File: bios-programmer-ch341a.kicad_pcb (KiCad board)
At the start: 2 copper layers, 50 x 56 mm, 28 parts, among them J1 USB_B_Micro, J4 +Banana+, J5 -Banana-, J6 ZIF16, J7 Conn_02x04_Counter_Clockwise, J8 Conn_02x04_Counter_Clockwise, SW1 RESET, U1 CH341A, U2 ISO6741, U3 ADuM1252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

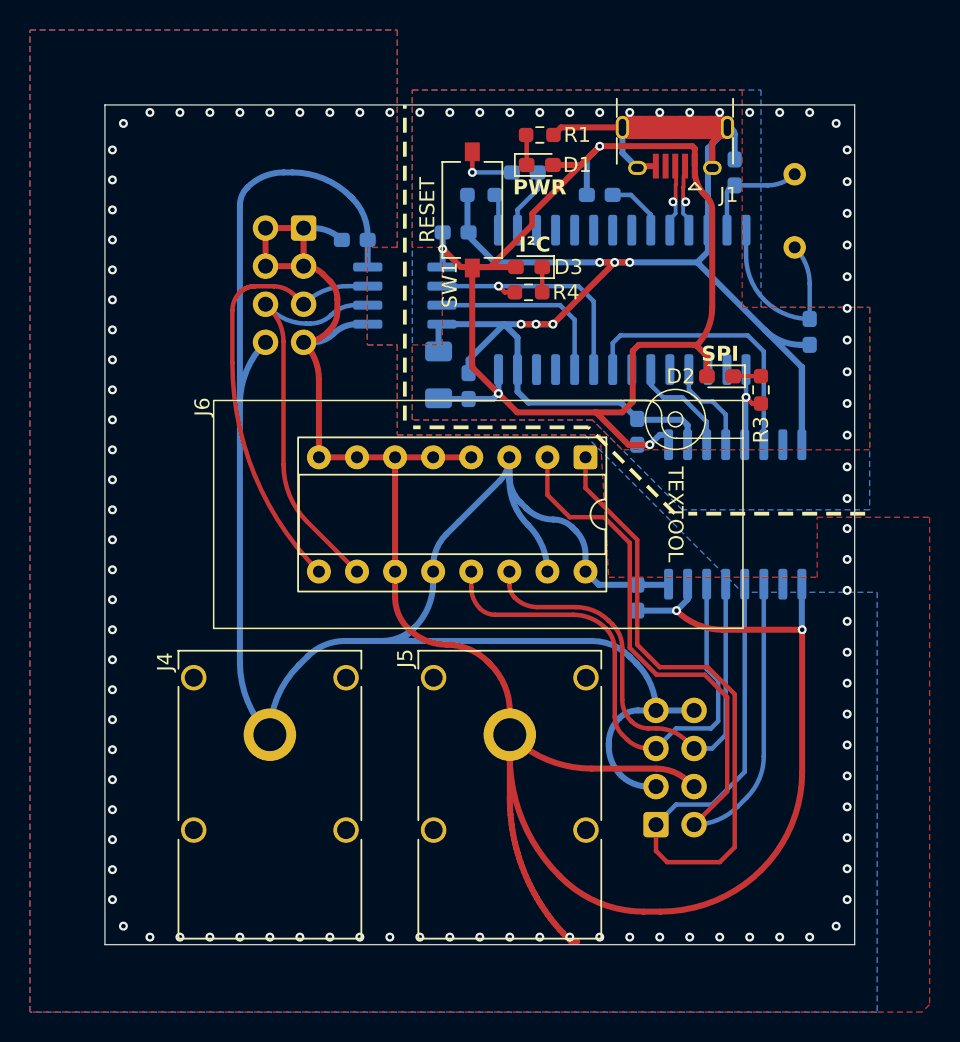
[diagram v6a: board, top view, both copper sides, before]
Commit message: PCB: added silkscreens for pin layout and found BIG ISSUE
These silkscreens are quite important simply to understand what the device does
and prevent mistakes. They need to be correct and placed in a way they can be
read easily without mistakes.

As I expected I seem to have made a mistake on at least the pinouts of the IDC
connectors. That's too bad since I'l have to reroute them after correcting this.
First things first however, I'm going to verify the pinout of both the IDC con-
nectors and the ZIF socket with every reference I have.

The worst thing that could happen - as it's hard to fix with an extra compoent
or a hookup wire - is a mistake in the pinouts. All of the PCBs that I order
will be a waste of both money and resources.
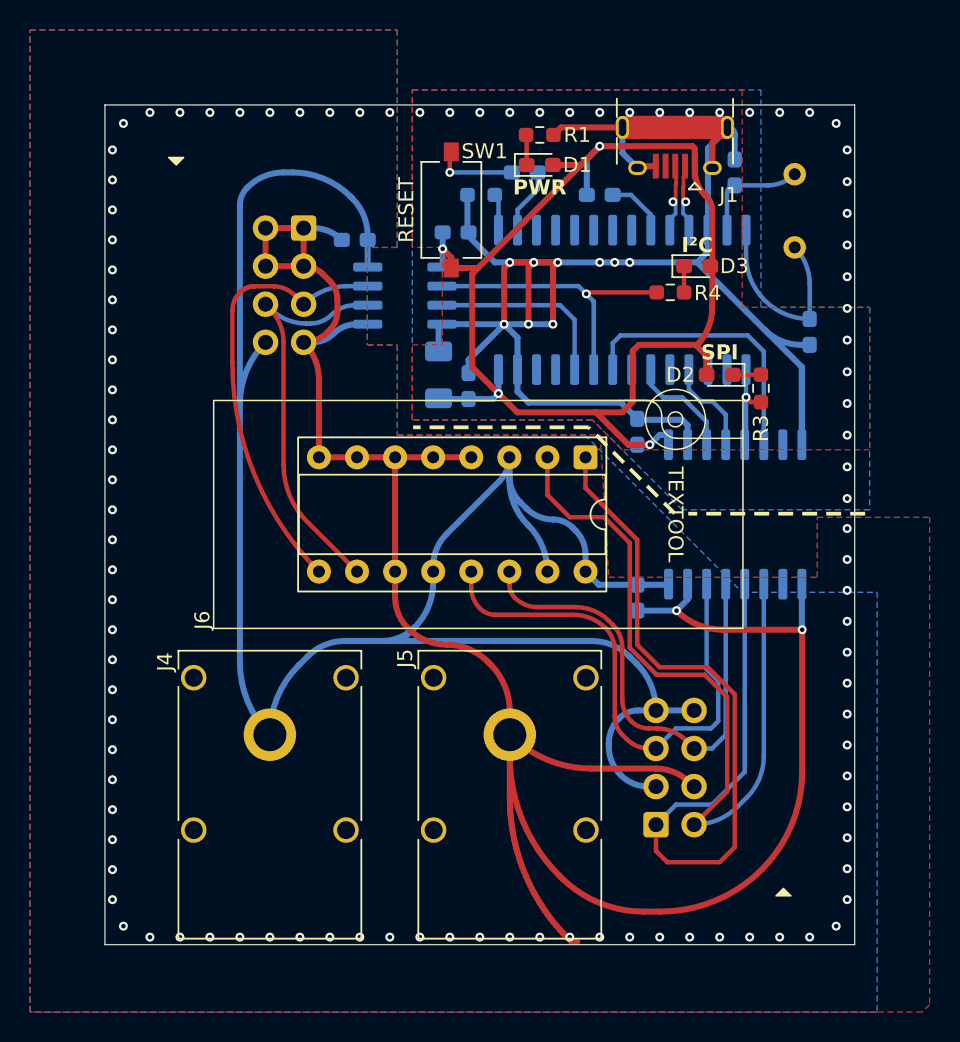
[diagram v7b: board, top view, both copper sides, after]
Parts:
- moved D3 11.2 mm to (79.5, 40.8), turned to 0 degrees
- moved R4 9.46 mm to (77.7, 42.5)
- moved SW1 1.40 mm to (63.1, 37.0)
- moved D2 0.10 mm to (81.0, 48.0)
- moved R3 0.10 mm to (83.8, 48.9)
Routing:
- net GND: track 222.2 -> 228.2 mm, vias 33 -> 36
- net /SDA: track 16.4 -> 19.8 mm
- net VBUS: track 88.6 -> 85.8 mm
- net /RST: track 4.01 -> 5.51 mm
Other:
- board text removed: "reset switch kleiner ring rondom rond, niet connected? of toch GND? maar welke? 2 halve ringen? misschien beter 2 zones, tot bijna tegen elkaar?"

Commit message: SCH/PCB: corrected external pinouts - hopefully correct now
First part that was wrong was the footprint vs symbol which didn't have a
compatible pin numbering. Then aside from that there were still mistakes that
lead to wrong pinouts.
By rerouting the SPI signals it seems easiest to route them under the ZIF
socket, which I've been able to prevent previous time. Not that that's much of
an issue as far as I can estimate.

The silkscreen legend for the ZIF socket was also wrong, somehow I still have
the layout from the off-the-shelf programmers (with 24xx on top) in my mind.
This is definitely one of the downsides of changing this, but also show the
importance of having good silkscreen legends.
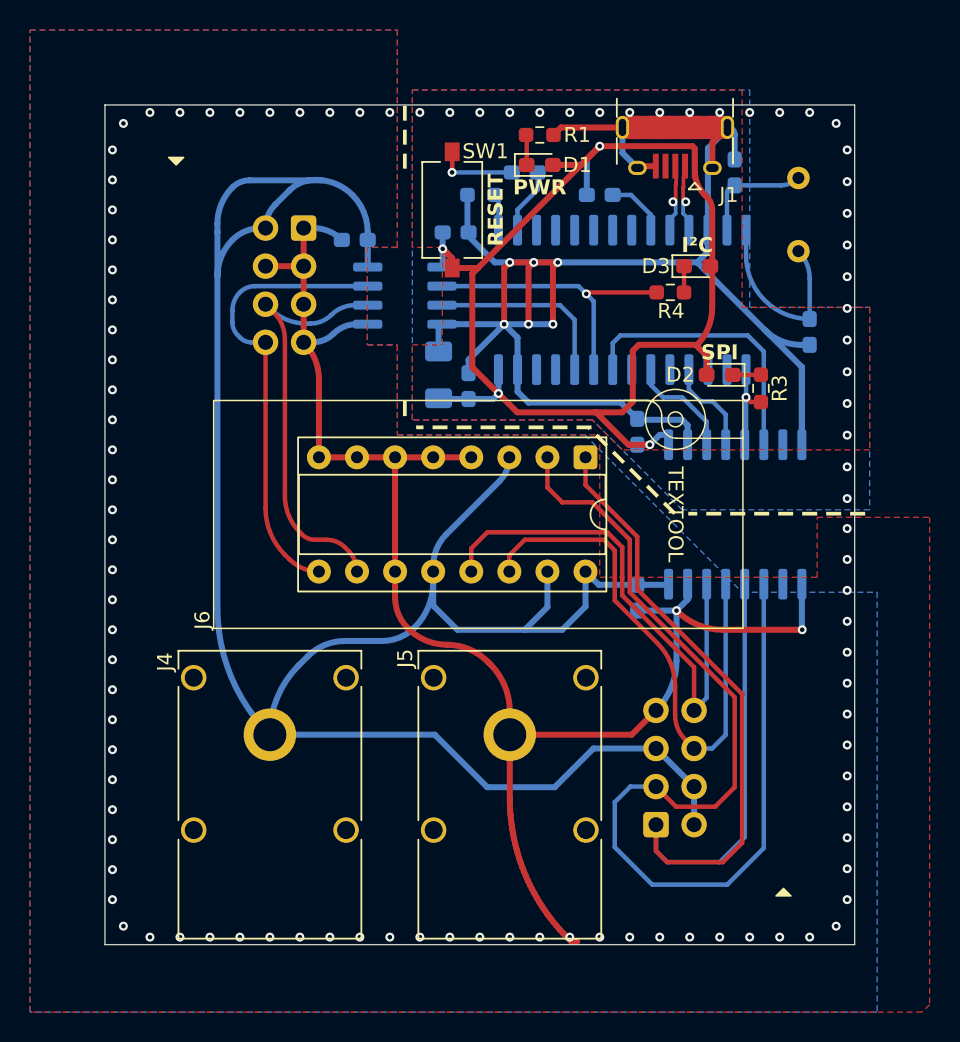
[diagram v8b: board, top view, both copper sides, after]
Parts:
- moved Y1 0.35 mm to (86.2, 39.8)
- moved SW1 0.06 mm to (63.2, 37.0)
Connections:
- J7 pad 2: /MISO_I -> VDD
- J7 pad 3: VDD -> /MISO_I
- J7 pad 4: GNDD -> VDD
- J7 pad 5: /MOSI_I -> VDD
- J7 pad 7: VDD -> GNDD
- J7 pad 8: VDD -> /MOSI_I
- J8 pad 2: GNDD -> VDD
- J8 pad 5: /SDA_I -> GNDD
- J8 pad 8: VDD -> /SDA_I
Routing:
- net GNDD: track 443.6 -> 398.9 mm
- net /MISO_I: track 51.5 -> 70.5 mm
- net VDD: track 142.0 -> 149.3 mm
- net /CS_I: track 58.9 -> 63.9 mm
- net /CLK_I: track 32.1 -> 35.8 mm
- net VBUS: track 85.8 -> 89.0 mm
- net /SCL_I: track 27.0 -> 28.1 mm
- net /MOSI_I: track 34.9 -> 34.1 mm
- net GND: vias 36 -> 33
